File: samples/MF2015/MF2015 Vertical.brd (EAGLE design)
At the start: 88.9 x 50.8 mm, 48 parts, among them IC1 LPC11U24FBD48/401, Q2 BC857B, Y2 12MHz

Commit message: Lots of work on layout and routing of the MF board.
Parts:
- removed U$1, U$2, U$3, U$4: FIDUCIAL, adafruit:FIDUCIAL_1MM
- removed Y2: 12MHz, microbuilder:CRYSTAL_2.5X2
- added BAT1, BAT2: (no value), SparkFun-Electromechanical:BATTERY-AAA-KIT
- added FID1, FID2, FID3, FID4: FIDUCIAL1X2, SparkFun-Aesthetics:FIDUCIAL-1X2
- added IC2: LD117AS12TR, v-reg:SOT223
- added IC3: TPS61200, texas:S-PDSO-N10
- added Q1: (no value), JVN:CRYSTAL-SMD-5X3.2-2PIN
- added R3: 1M, rcl:R0603
- R11, R2, R5: value 10k -> 10K
- R14: value 1.5k -> 1.5K
- R15: value 3k -> 3K
- R16: value 24k -> 24K
- moved L21 43.7 mm to (39.4, 47.0), turned to 0 degrees
- moved L16 43.6 mm to (39.4, 36.8), turned to 0 degrees
- moved L11 43.6 mm to (39.4, 26.7), turned to 0 degrees
- moved L6 43.6 mm to (39.4, 16.5), turned to 0 degrees
- moved L1 43.6 mm to (39.4, 6.35), turned to 0 degrees
- moved L25 37.1 mm to (80.0, 47.0), turned to 0 degrees
- moved L20 37.0 mm to (80.0, 36.8), turned to 0 degrees
- moved L15 37.0 mm to (80.0, 26.7), turned to 0 degrees
- moved L10 37.0 mm to (80.0, 16.5), turned to 0 degrees
- moved L5 37.0 mm to (80.0, 6.35), turned to 0 degrees
- moved R12 34.2 mm to (26.7, 40.6)
- moved R2 30.8 mm to (3.81, 15.2), turned to 180 degrees
- moved S4 30.8 mm to (3.81, 10.2), turned to 90 degrees
- moved R11 30.4 mm to (3.81, 38.1), turned to 180 degrees
- moved S3 30.4 mm to (3.81, 43.2), turned to 90 degrees
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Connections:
- new net +: BAT1.PWR@1
- new net N$34: R3.2, U$5.4
- new net N$37: BAT1.GND@1, BAT2.PWR@1
- new net N$38: IC1.25, L1.4-DIN
- new net PGND: IC3.4
- new net PP: IC3.PP, IC3.PP@1, IC3.PP@2
- net GND: now also BAT2.GND@1, IC3.9, R3.1
- net N$25: now also Q1.P$2; no longer Y2.1
- net N$26: now also Q1.P$1; no longer Y2.3
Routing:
- net N$45: track 0.00 -> 245.5 mm
- net N$5: track 0.00 -> 51.1 mm
- net N$10: track 0.00 -> 51.1 mm
- net N$25: track 18.0 -> 0.00 mm
- net N$26: track 14.6 -> 0.00 mm
- net N$9: track 0.00 -> 6.80 mm
- net N$8: track 0.00 -> 6.80 mm
- net N$7: track 0.00 -> 6.80 mm
- net N$4: track 0.00 -> 6.80 mm
- net N$3: track 0.00 -> 6.80 mm
- net N$2: track 0.00 -> 6.80 mm
- net N$6: track 0.00 -> 6.80 mm
- net N$1: track 0.00 -> 6.80 mm
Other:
- board size 88.9 x 50.8 mm -> 85.6 x 54 mm
- board text removed: "Open Source SMT"
- board text removed: "OpenPnP"
- board text removed: "Pick and Place"
- board text removed: "http://openpnp.org"

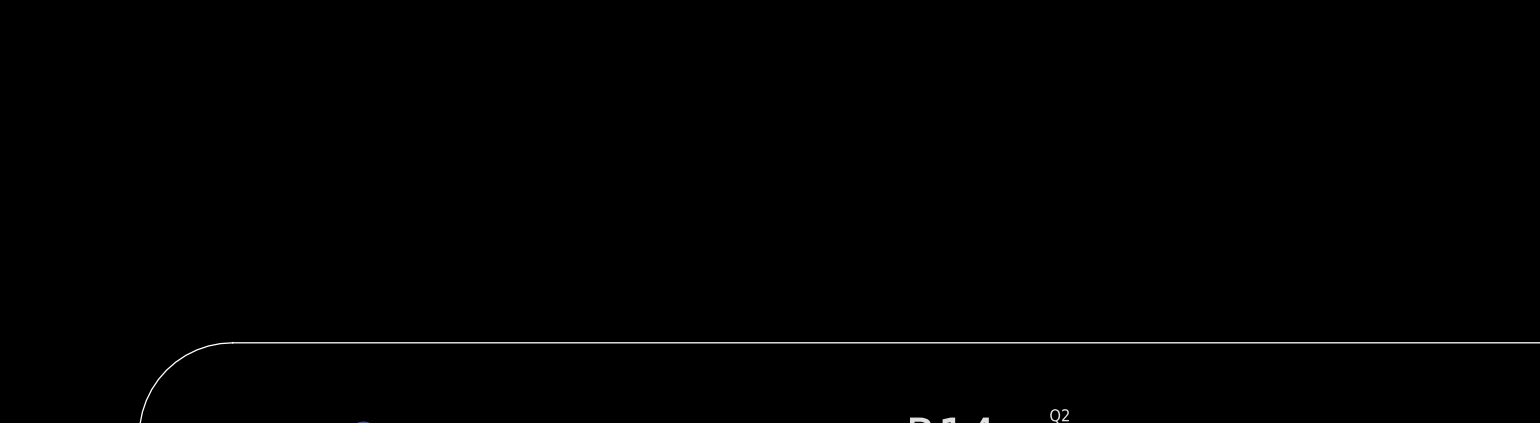
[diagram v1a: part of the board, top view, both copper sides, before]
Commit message: Errata updates to the demo boards.
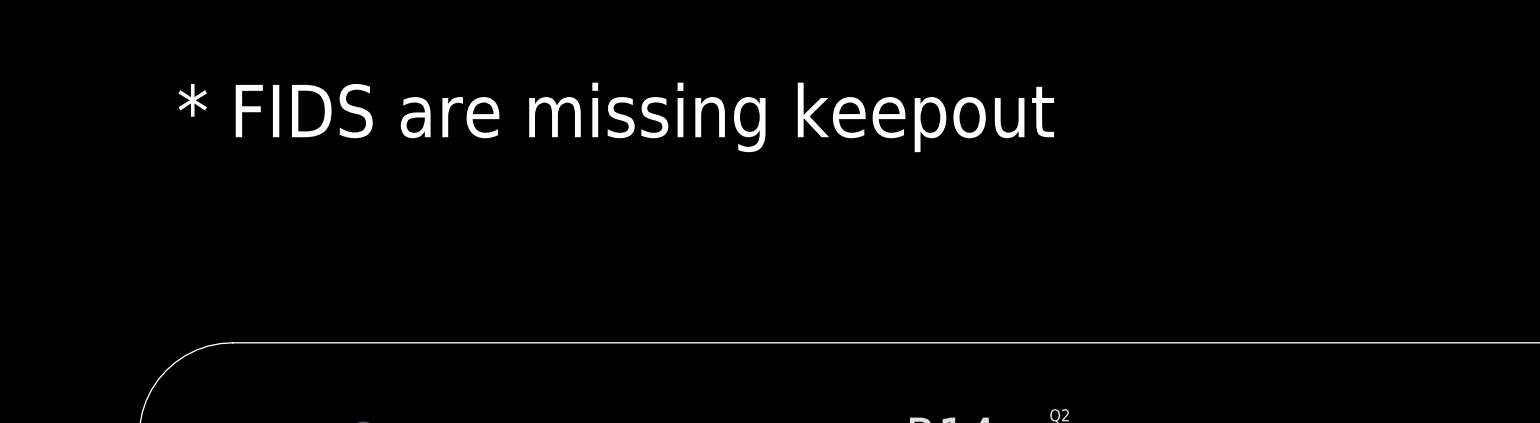
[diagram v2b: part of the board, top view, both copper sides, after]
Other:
- board text added: "* FIDS are missing keepout"
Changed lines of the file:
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@@
 <rectangle x1="10.8966" y1="8.0518" x2="11.2014" y2="8.0772" layer="200" rot="R90"/>
 <rectangle x1="10.9093" y1="9.3091" x2="11.1887" y2="9.3345" layer="200" rot="R90"/>
+<text x="1.27" y="60.96" size="1.778" layer="20">* FIDS are missing keepout</text>
 </plain>
 <attributes>
